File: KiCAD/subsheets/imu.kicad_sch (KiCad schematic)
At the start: 4 parts, among them U8 LSM6DS3

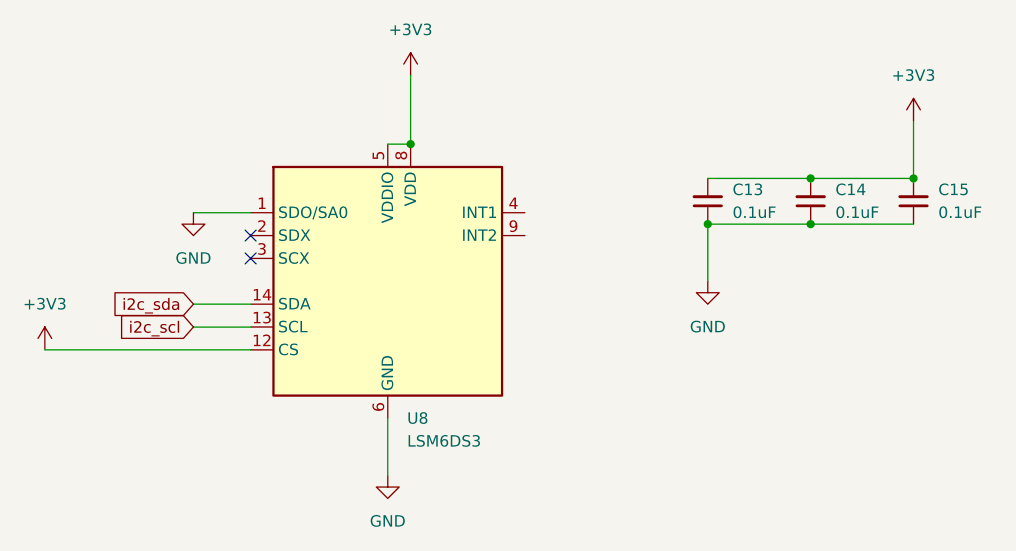
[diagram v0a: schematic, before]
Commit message: connect forgotten pins
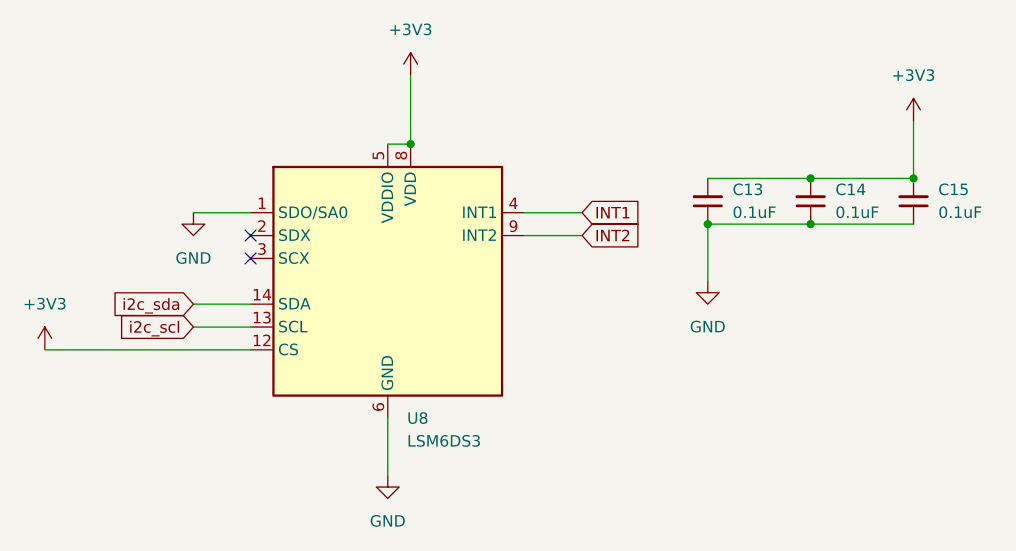
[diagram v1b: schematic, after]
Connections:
- net INT1: now reaches U8.4 (INT1)
- net INT2: now reaches U8.9 (INT2)
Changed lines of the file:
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@@
+	(wire
+		(pts
+			(xy 160.02 93.98) (xy 166.37 93.98)
+		)
+		(stroke
+			(width 0)
+			(type default)
+		)
+	)
 	(wire
 		(pts
@@
 	(wire
 		(pts
+			(xy 160.02 96.52) (xy 166.37 96.52)
+		)
+		(stroke
+			(width 0)
+			(type default)
+		)
+	)
+	(wire
+		(pts
 			(xy 106.68 109.22) (xy 129.54 109.22)
 		)
@@
 		)
 	)
+	(global_label "INT2"
+		(shape input)
+		(at 166.37 96.52 0)
+		(fields_autoplaced yes)
+		(effects
+			(font
+				(size 1.27 1.27)
+			)
+			(justify left)
+		)
+		(property "Intersheetrefs" "${INTERSHEET_REFS}"
+			(at 173.4676 96.52 0)
+			(hide yes)
+			(show_name no)
+			(do_not_autoplace no)
+			(effects
+				(font
+					(size 1.27 1.27)
+				)
+				(justify left)
+			)
+		)
+	)
 	(global_label "i2c_sda"
 		(shape input)
@@
 			)
 		)
+	)
+	(global_label "INT1"
+		(shape input)
+		(at 166.37 93.98 0)
+		(fields_autoplaced yes)
+		(effects
+			(font
+				(size 1.27 1.27)
+			)
+			(justify left)
+		)
+		(property "Intersheetrefs" "${INTERSHEET_REFS}"
+			(at 173.4676 93.98 0)
+			(hide yes)
+			(show_name no)
+			(do_not_autoplace no)
+			(effects
+				(font
+					(size 1.27 1.27)
+				)
+				(justify left)
+			)
+		)
